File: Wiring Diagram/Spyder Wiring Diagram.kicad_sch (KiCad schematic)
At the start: 19 parts, among them U1 MPU-6050, U2 NRF24L01

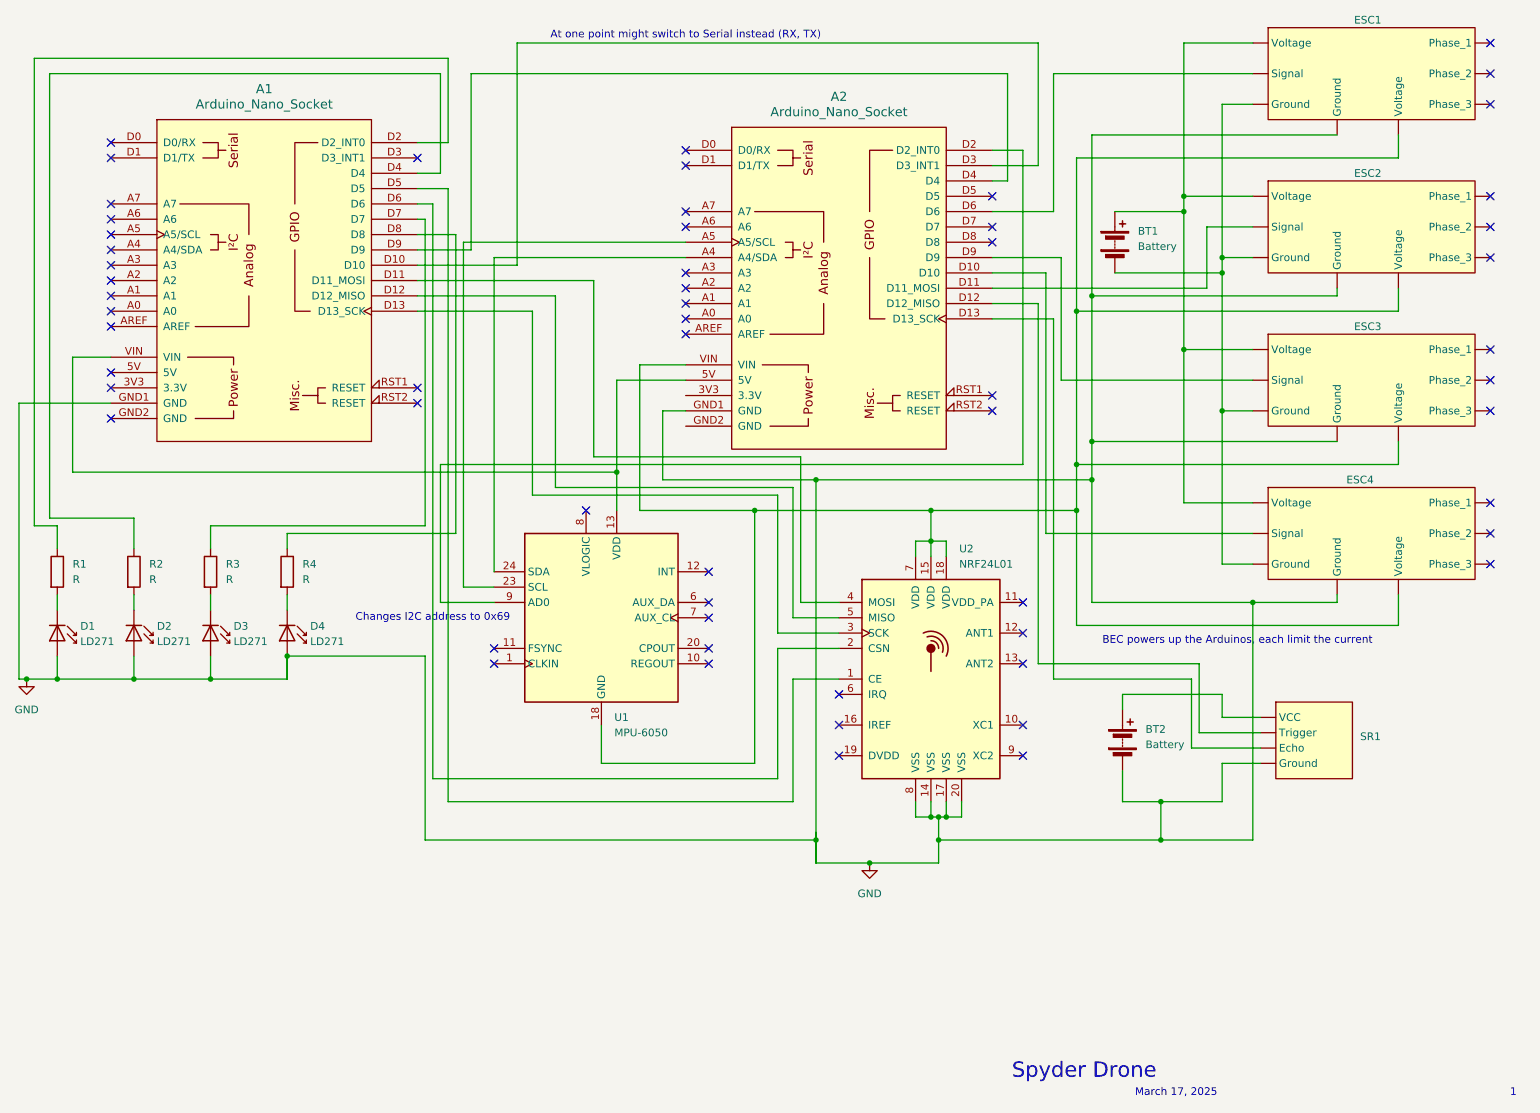
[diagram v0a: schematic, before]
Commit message: Update wiring diagram with S2 developments.
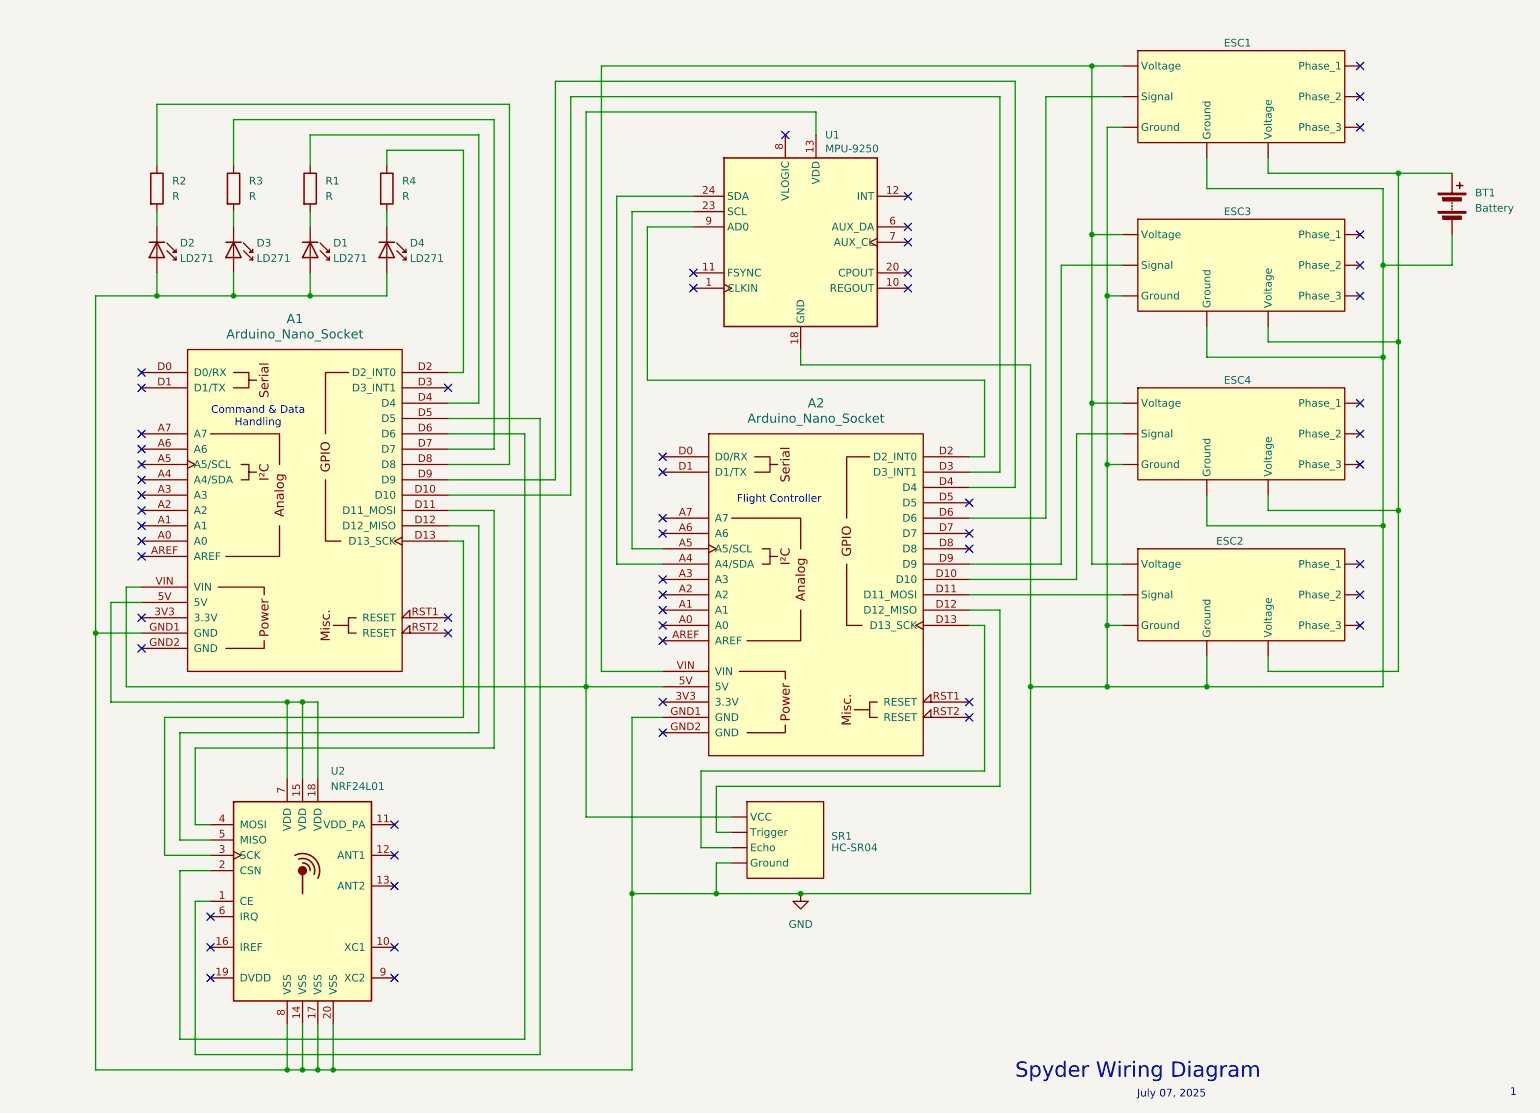
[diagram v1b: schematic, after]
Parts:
- removed BT2: Battery, symbol Device:Battery
- SR1: value ~ -> HC-SR04
- U1: value MPU-6050 -> MPU-9250
- renumbered D3 to D1, D1 to D2, D2 to D3, ESC4 to ESC2, ESC2 to ESC3, ESC3 to ESC4, R3 to R1, R1 to R2, R2 to R3
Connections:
- net GND: now also BT1.2 (-), U1.18 (GND)
- net at R2.1: now also A1.D8; no longer A1.D2 (D2_INT0)
- net at A2.D9: now also ESC3. (Phase_3); no longer ESC4. (Phase_3)
- net at A1.VIN, A2.5V, U1.13 (VDD): now also SR1. (Ground)
- net at A1.5V: now also U2.15 (VDD), U2.18 (VDD), U2.7 (VDD)
- net at A1.D4: now also R1.1; no longer R3.1
- net at A1.D7: now also R3.1; no longer R1.1
- net at R4.1: now also A1.D2 (D2_INT0); no longer A1.D8
- net at A2.D11 (D11_MOSI): now also ESC2. (Phase_3); no longer ESC3. (Phase_3)
- net at A2.D10: now also ESC4. (Phase_3); no longer ESC2. (Phase_3)
- new net: BT1.1 (+), ESC1. (Phase_3), ESC2. (Phase_3), ESC3. (Phase_3), ESC4. (Phase_3)
- new net: A2.VIN, ESC1. (Phase_3), ESC2. (Phase_3), ESC3. (Phase_3), ESC4. (Phase_3)
- no-connect marks 59 -> 60
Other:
- note added: "Command & Data Handling"
- note added: "Flight Controller"
- note added: "July 07, 2025"
- note added: "Spyder Wiring Diagram"
- note removed: "At one point might switch to Serial instead (RX, TX)"
- note removed: "BEC powers up the Arduinos, each limit the current"
- note removed: "Changes I2C address to 0x69"
- note removed: "March 17, 2025"
- note removed: "Spyder Drone"
- moved on the sheet: A1, A2, BT1, D1, D2, D3, D4, ESC1, ESC2, ESC3, ESC4, R1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
